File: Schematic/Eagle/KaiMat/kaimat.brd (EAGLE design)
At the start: 60 x 110.5 mm, 63 parts, among them IC1 TL074CN, IC2 TL074CN

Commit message: better pcb
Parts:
- moved R39 271.4 mm to (58.0, 104.0), turned to 90 degrees
- moved R36 260.1 mm to (50.0, 104.5), turned to 90 degrees
- moved R33 247.6 mm to (40.0, 104.0), turned to 90 degrees
- moved R30 235.9 mm to (30.0, 104.0), turned to 90 degrees
- moved R24 194.2 mm to (30.0, 89.5), turned to 90 degrees
- moved R18 175.2 mm to (40.0, 89.5), turned to 90 degrees
- moved D2 135.1 mm to (55.5, 7.00), flipped to the bottom, turned to 90 degrees
- moved R2 114.2 mm to (20.0, 104.2), turned to 90 degrees
- moved R4 107.1 mm to (20.0, 90.0), turned to 90 degrees
- moved R1 106.3 mm to (9.90, 104.2), turned to 90 degrees
- moved R3 102.1 mm to (10.0, 89.5), turned to 90 degrees
- moved R9 88.5 mm to (18.5, 54.0), turned to 90 degrees
- moved R10 86.2 mm to (16.0, 55.5), turned to 90 degrees
- moved R11 71.5 mm to (11.8, 34.2), turned to 270 degrees
- moved R6 65.4 mm to (18.5, 44.5), turned to 270 degrees
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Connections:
- net DACOUTCV2: now also U$5.5; no longer U$5.13
- net DACOUTCV3: now also U$5.6; no longer U$5.5
- net DACOUTCV4: now also U$5.7; no longer U$5.12
- net DACOUTTR1: now also U$5.13; no longer U$5.6
- net DACOUTTR2: now also U$5.12; no longer U$5.11
- net DACOUTTR3: now also U$5.11; no longer U$5.7
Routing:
- net ENC2SW: track 0.00 -> 67.7 mm, vias 0 -> 2
- net ENC2PINB: track 0.00 -> 58.4 mm, vias 0 -> 1
- net OLEDCLK: track 0.00 -> 58.1 mm, vias 0 -> 1
- net OLEDDATA: track 0.00 -> 54.9 mm, vias 0 -> 1
- net N$29: track 0.00 -> 54.7 mm
- net ENC2PINA: track 0.00 -> 53.9 mm, vias 0 -> 1
- net OLEDDC: track 0.00 -> 52.7 mm, vias 0 -> 1
- net OLEDCS: track 0.00 -> 52.1 mm, vias 0 -> 3
- net OLEDRST: track 0.00 -> 48.3 mm, vias 0 -> 2
- net +5V: track 6.01 -> 53.6 mm
- net B2: track 6.50 -> 48.2 mm
- net ENC1SW: track 0.00 -> 41.0 mm
- net ENC1PINA: track 0.00 -> 37.8 mm
- net B1: track 6.50 -> 42.5 mm
- net ENC1PINB: track 0.00 -> 32.1 mm
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
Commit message: better pcb
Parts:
- moved R21 187.7 mm to (50.0, 89.5), turned to 90 degrees
- moved R27 174.6 mm to (58.0, 52.5), turned to 90 degrees
- moved R35 156.0 mm to (2.50, 8.00), turned to 90 degrees
- moved R12 71.6 mm to (18.8, 29.7), turned to 270 degrees
- moved R8 65.3 mm to (15.0, 38.0)
- moved R39 39.0 mm to (58.0, 65.0)
- moved U$5 28.0 mm to (44.0, 13.5), turned to 180 degrees
- moved IC1 6.10 mm to (52.4, 27.5), turned to 0 degrees
- moved IC2 4.92 mm to (50.5, 47.5), turned to 0 degrees
- moved R11 4.92 mm to (9.80, 29.7)
- moved U$2 1.58 mm to (16.9, 10.1)
- moved D1 1.50 mm to (7.42, 19.8)
- moved OPAMP1 1.00 mm to (9.50, 50.5)
- moved R7 1.00 mm to (6.00, 39.0)
- flipped R1 to the bottom
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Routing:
- net VCC: track 1.76 -> 114.6 mm, vias 0 -> 2
- net N$14: track 0.00 -> 61.1 mm, vias 0 -> 1
- net DACCLR: track 0.00 -> 54.3 mm
- net N$11: track 0.00 -> 53.9 mm
- net GND: track 342.8 -> 393.0 mm
- net N$16: track 0.00 -> 49.0 mm
- net N$40: track 0.00 -> 46.7 mm
- net DACDATA: track 0.00 -> 44.1 mm
- net DACSPICLK: track 0.00 -> 42.9 mm
- net DACSS: track 0.00 -> 37.6 mm
- net N$15: track 0.00 -> 37.5 mm
- net DACLDAC: track 0.00 -> 34.7 mm
- net N$28: track 0.00 -> 31.2 mm
- net +5V: track 53.6 -> 70.4 mm
- net CVIN4: track 0.00 -> 14.1 mm
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
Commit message: better pcb
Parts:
- moved R28 183.1 mm to (42.5, 55.5), turned to 270 degrees
- moved IC2 2.55 mm to (50.0, 50.0)
- flipped R35 to the bottom
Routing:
- net N$27: track 0.00 -> 15.0 mm
- net +5V: track 70.4 -> 76.5 mm
- net N$39: track 0.00 -> 5.51 mm
- net VCC: track 114.6 -> 117.3 mm
- net VSS: track 42.0 -> 44.1 mm
- net DACSS: track 37.6 -> 38.6 mm
- net N$1: track 14.0 -> 14.8 mm
- net ENC2SW: track 72.1 -> 71.5 mm

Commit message: better pcb
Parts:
- removed R37, R38, R39: 100k, MusicThingModular:7MM_RESISTOR
- removed U$5: DAC8568C, analog-devices-3:TSSOP16
- added DAC8568C: DAC8568C, analog-devices-3:TSSOP16
- added R13, R14, R15: 100k, Clean-Kong:R0805
- R1, R10, R11, R12, R16, R17, R18, R19, R2, R20, R21, R22, R23, R24, R25, R26, R27, R28, R29, R3, R30, R31, R32, R33, R34, R35, R36, R4, R5, R6, R7, R8, R9: device MusicThingModular:7MM_RESISTOR -> Clean-Kong:R0805
- moved R34 207.5 mm to (49.5, 58.0), flipped to the bottom, turned to 90 degrees
- moved R31 198.8 mm to (55.5, 58.0), flipped to the bottom, turned to 270 degrees
- moved R29 185.7 mm to (49.5, 53.0), flipped to the bottom, turned to 90 degrees
- moved R32 183.2 mm to (49.5, 40.0), flipped to the bottom, turned to 270 degrees
- moved R25 157.2 mm to (42.0, 46.0), flipped to the bottom
- moved R26 151.8 mm to (53.5, 33.5), flipped to the bottom, turned to 270 degrees
- moved R22 141.2 mm to (42.0, 40.0), flipped to the bottom, turned to 180 degrees
- moved R23 140.9 mm to (50.5, 33.5), flipped to the bottom, turned to 90 degrees
- moved R20 137.4 mm to (42.0, 43.0), flipped to the bottom
- moved R16 118.3 mm to (42.0, 37.0), flipped to the bottom, turned to 180 degrees
- moved R19 116.5 mm to (53.5, 20.0), flipped to the bottom, turned to 90 degrees
- moved R17 108.9 mm to (50.5, 20.0), flipped to the bottom, turned to 270 degrees
- moved R35 66.6 mm to (46.5, 58.0)
- moved R33 65.2 mm to (52.5, 40.0), flipped to the bottom
- moved R36 51.6 mm to (52.5, 53.0), flipped to the bottom, turned to 270 degrees
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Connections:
- net +5V: now also DAC8568C.3; no longer U$5.3
- net CVIN2: now also R9.2; no longer R9.1
- net CVIN3: now also R11.2; no longer R11.1
- net DACCLR: now also DAC8568C.9; no longer U$5.9
- net DACDATA: now also DAC8568C.15; no longer U$5.15
- net DACLDAC: now also DAC8568C.1; no longer U$5.1
- net DACOUTCV1: now also DAC8568C.4; no longer U$5.4
- net DACOUTCV2: now also DAC8568C.5; no longer U$5.5
- net DACOUTCV3: now also DAC8568C.6; no longer U$5.6
- net DACOUTCV4: now also DAC8568C.7; no longer U$5.7
- net DACOUTTR1: now also DAC8568C.13; no longer U$5.13
- net DACOUTTR2: now also DAC8568C.12; no longer U$5.12
- net DACOUTTR3: now also DAC8568C.11; no longer U$5.11
- net DACOUTTR4: now also DAC8568C.10; no longer U$5.10
- net DACSPICLK: now also DAC8568C.16; no longer U$5.16
- net DACSS: now also DAC8568C.2; no longer U$5.2
- net ENC1PINA: now also U$1.15/A1; no longer U$1.1/TX
- net ENC1PINB: now also U$1.16/A2; no longer U$1.2
- net ENC1SW: now also U$1.14/A0; no longer U$1.0/RX
- net ENC2PINA: now also U$1.1/TX; no longer U$1.15/A1
- net ENC2PINB: now also U$1.2; no longer U$1.16/A2
- net ENC2SW: now also U$1.0/RX; no longer U$1.14/A0
- net GND: now also DAC8568C.14, R11.1, R34.2, R9.1; no longer R11.2, R37.2, R9.2, U$5.14
- net N$11: now also R2.2; no longer R2.1
- net N$15: now also R3.2; no longer R3.1
- net N$31: now also R13.1; no longer R30.1
- net N$33: now also R13.2; no longer R30.2
- net N$34: now also R14.2; no longer R33.2
- net N$35: now also R33.2, R34.1; no longer R34.2, R35.1
- net N$36: now also R30.2; no longer R36.2
- net N$37: now also R30.1, R33.1; no longer R34.1, R36.1
- net N$38: now also R35.1, R36.2; no longer R37.1, R38.2
- net N$39: now also R15.1, R36.1; no longer R38.1, R39.1
- net N$40: now also R15.2; no longer R39.2
- net N$5: now also R2.1; no longer R2.2
- net N$6: now also R3.1; no longer R3.2
- net N$7: now also R14.1; no longer R33.1
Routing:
- net N$14: track 61.1 -> 0.00 mm, vias 1 -> 0
- net N$11: track 53.9 -> 0.00 mm
- net N$16: track 49.0 -> 0.00 mm
- net N$40: track 46.7 -> 7.53 mm
- net ENC2SW: track 71.5 -> 34.0 mm, vias 2 -> 0
- net N$15: track 37.5 -> 0.00 mm
- net VCC: track 117.3 -> 79.9 mm, vias 2 -> 1
- net ENC1SW: track 41.0 -> 75.4 mm
- net ENC2PINA: track 53.9 -> 20.4 mm, vias 2 -> 0
- net ENC1PINA: track 37.8 -> 61.0 mm
- net ENC2PINB: track 59.4 -> 36.5 mm, vias 4 -> 0
- net N$28: track 31.0 -> 8.11 mm
- net N$17: track 0.00 -> 22.5 mm
- net N$4: track 27.7 -> 5.45 mm
- net ENC1PINB: track 32.1 -> 52.7 mm
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
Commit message: finished pcb
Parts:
- moved R16 18.5 mm to (42.0, 18.5)
- moved R6 14.9 mm to (8.50, 43.0), turned to 270 degrees
- moved R5 14.2 mm to (9.50, 57.0), turned to 0 degrees
- moved R22 13.5 mm to (42.0, 26.5)
- moved R7 12.6 mm to (16.0, 47.0), turned to 90 degrees
- moved R20 7.00 mm to (42.0, 36.0)
- moved R34 6.50 mm to (56.0, 58.0)
- moved R28 6.00 mm to (46.5, 58.0)
- moved R31 6.00 mm to (49.5, 58.0)
- moved R35 6.00 mm to (52.5, 58.0)
- moved R10 5.00 mm to (3.00, 56.0)
- moved R11 5.00 mm to (3.00, 51.0)
- moved R25 4.50 mm to (42.0, 41.5)
- moved R8 2.50 mm to (11.5, 43.0), turned to 270 degrees
- moved DAC8568C 1.50 mm to (46.0, 12.0)
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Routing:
- net N$11: track 0.00 -> 95.5 mm, vias 0 -> 1
- net N$21: track 2.47 -> 82.3 mm, vias 0 -> 1
- net N$37: track 0.00 -> 76.2 mm, vias 0 -> 1
- net N$2: track 2.69 -> 77.7 mm, vias 0 -> 1
- net N$7: track 0.00 -> 74.4 mm, vias 0 -> 1
- net N$24: track 0.00 -> 69.7 mm, vias 0 -> 1
- net N$39: track 0.00 -> 61.6 mm, vias 0 -> 1
- net N$27: track 0.00 -> 59.6 mm, vias 0 -> 1
- net N$31: track 0.00 -> 58.6 mm, vias 0 -> 1
- net N$14: track 0.00 -> 57.4 mm, vias 0 -> 1
- net DACOUTTR1: track 0.00 -> 53.3 mm, vias 0 -> 2
- net GND: track 377.6 -> 429.2 mm, vias 4 -> 5
- net DACOUTTR2: track 0.00 -> 50.5 mm, vias 0 -> 2
- net DACOUTCV4: track 0.00 -> 47.7 mm, vias 0 -> 1
- net N$15: track 0.00 -> 45.1 mm, vias 0 -> 1
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
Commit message: better pcb
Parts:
- MCP6004-E_P: value MCP6004-E_P -> (none)
- TL04CN-1, TL04CN-2: value TL074CN -> (none)
- moved D1 0.50 mm to (7.69, 22.3)
- moved D2 0.50 mm to (55.0, 7.00)
- moved R7 0.50 mm to (16.5, 47.0)
- moved SV1 0.50 mm to (7.60, 9.12)
- moved U$2 0.50 mm to (14.9, 10.1)
- renumbered IC1 to TL04CN-2, IC2 to TL04CN-1, OPAMP1 to MCP6004-E_P, U$3 to SSD1306-128X64
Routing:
- net GND: track 429.2 -> 563.5 mm
- net N$1: track 11.8 -> 17.2 mm
- net N$29: track 51.2 -> 56.0 mm
- net ENC2PINB: track 36.5 -> 34.1 mm
- net OLEDRST: track 47.9 -> 50.2 mm
- net ENC2SW: track 34.0 -> 32.6 mm
- net VSS: track 42.0 -> 40.7 mm
- net VCC: track 106.1 -> 107.3 mm
- net DACLDAC: track 39.2 -> 40.4 mm
- net DACOUTTR2: track 50.5 -> 49.5 mm
- net +5V: track 106.3 -> 107.3 mm
- net DACCLR: track 37.0 -> 36.1 mm
- net CVIN2: track 31.0 -> 31.9 mm
- net N$16: track 42.1 -> 41.2 mm
- net ENC1PINB: track 54.1 -> 55.0 mm
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
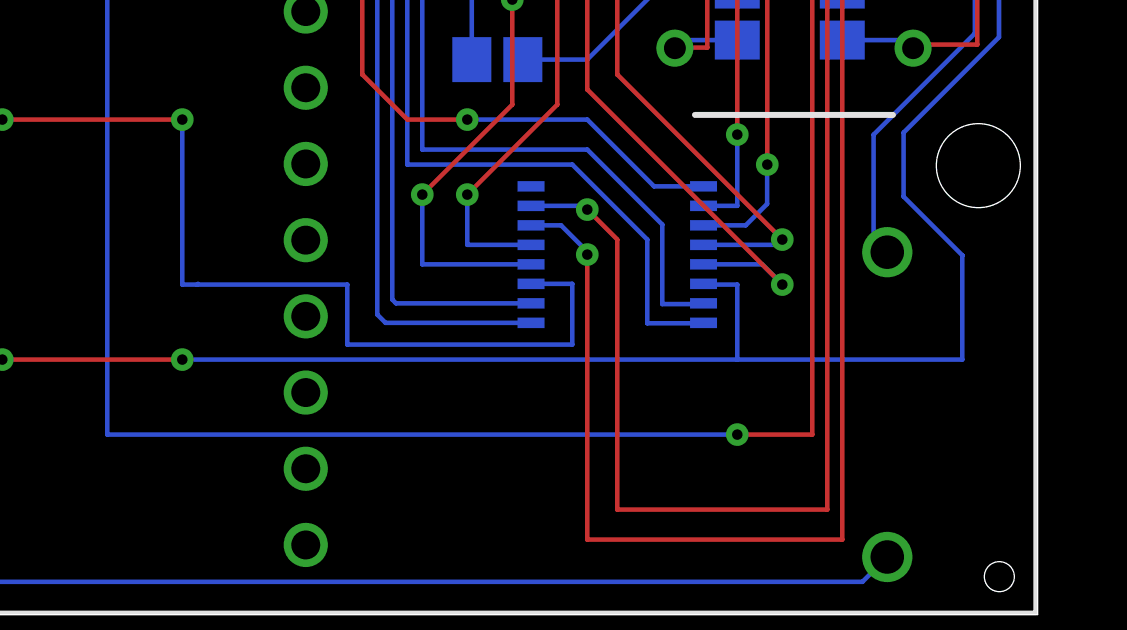
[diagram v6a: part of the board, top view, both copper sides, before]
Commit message: better oled speed and better code
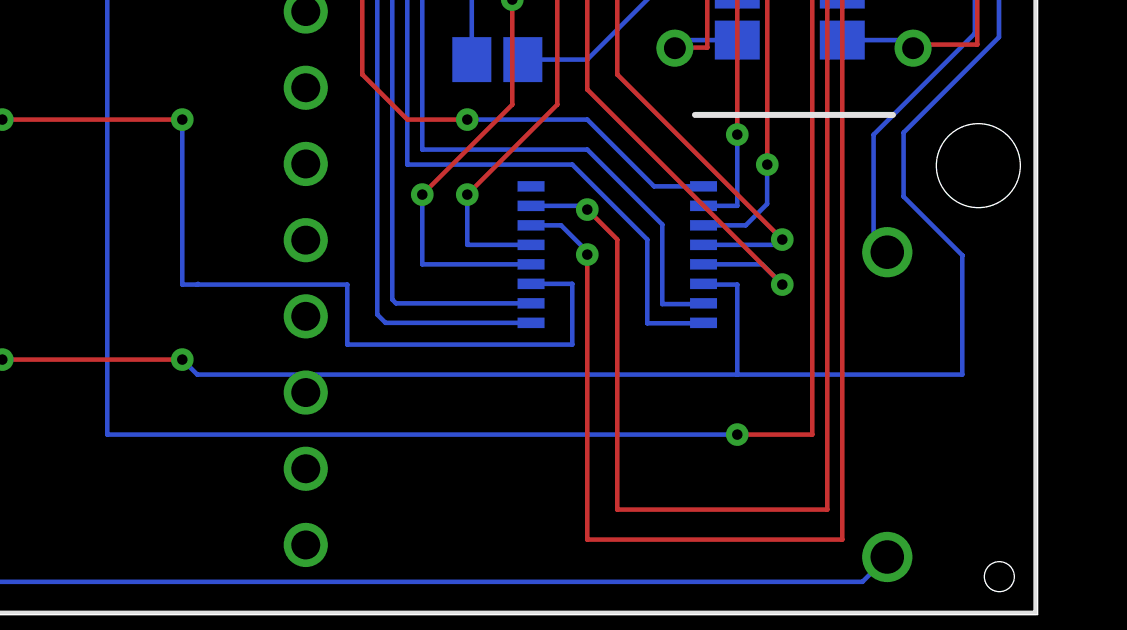
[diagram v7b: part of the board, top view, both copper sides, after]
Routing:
- net GND: track 563.5 -> 564.7 mm
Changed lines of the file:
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@@
 <drawing>
 <settings>
-<setting alwaysvectorfont="yes"/>
+<setting alwaysvectorfont="no"/>
 <setting verticaltext="up"/>
 </settings>
@@
 <via x="31.5" y="8.5" extent="1-16" drill="0.35"/>
 <wire x1="48.9" y1="11" x2="48.875" y2="11.025" width="0.1524" layer="16"/>
-<wire x1="50" y1="8.5" x2="31.5" y2="8.5" width="0.1524" layer="16"/>
-<wire x1="50" y1="8.5" x2="50" y2="11" width="0.1524" layer="16"/>
+<wire x1="50" y1="8" x2="32" y2="8" width="0.1524" layer="16"/>
+<wire x1="32" y1="8" x2="31.5" y2="8.5" width="0.1524" layer="16"/>
+<wire x1="50" y1="8" x2="50" y2="11" width="0.1524" layer="16"/>
 <wire x1="48.85" y1="11" x2="48.875" y2="11.025" width="0.1524" layer="16"/>
 <wire x1="50" y1="11" x2="48.9" y2="11" width="0.1524" layer="16"/>
@@
 <wire x1="57.1433" y1="59.7235" x2="56.2698" y2="58.85" width="0.1524" layer="16"/>
 <wire x1="56.2698" y1="58.85" x2="56" y2="58.85" width="0.1524" layer="16"/>
-<wire x1="57.5" y1="8.5" x2="50" y2="8.5" width="0.1524" layer="16"/>
-<wire x1="57.5" y1="8.5" x2="57.5" y2="11.9723" width="0.1524" layer="16"/>
+<wire x1="57.5" y1="8" x2="50" y2="8" width="0.1524" layer="16"/>
+<wire x1="57.5" y1="8" x2="57.5" y2="11.9723" width="0.1524" layer="16"/>
 <wire x1="57.5" y1="11.9723" x2="57.50319375" y2="11.9723" width="0.1524" layer="16"/>
 <wire x1="57.50319375" y1="11.9723" x2="55.5433" y2="13.93219375" width="0.1524" layer="16"/>
